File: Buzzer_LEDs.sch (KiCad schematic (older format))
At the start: 15 parts, among them Q1 2N7002BK, Q2 2N7002BK

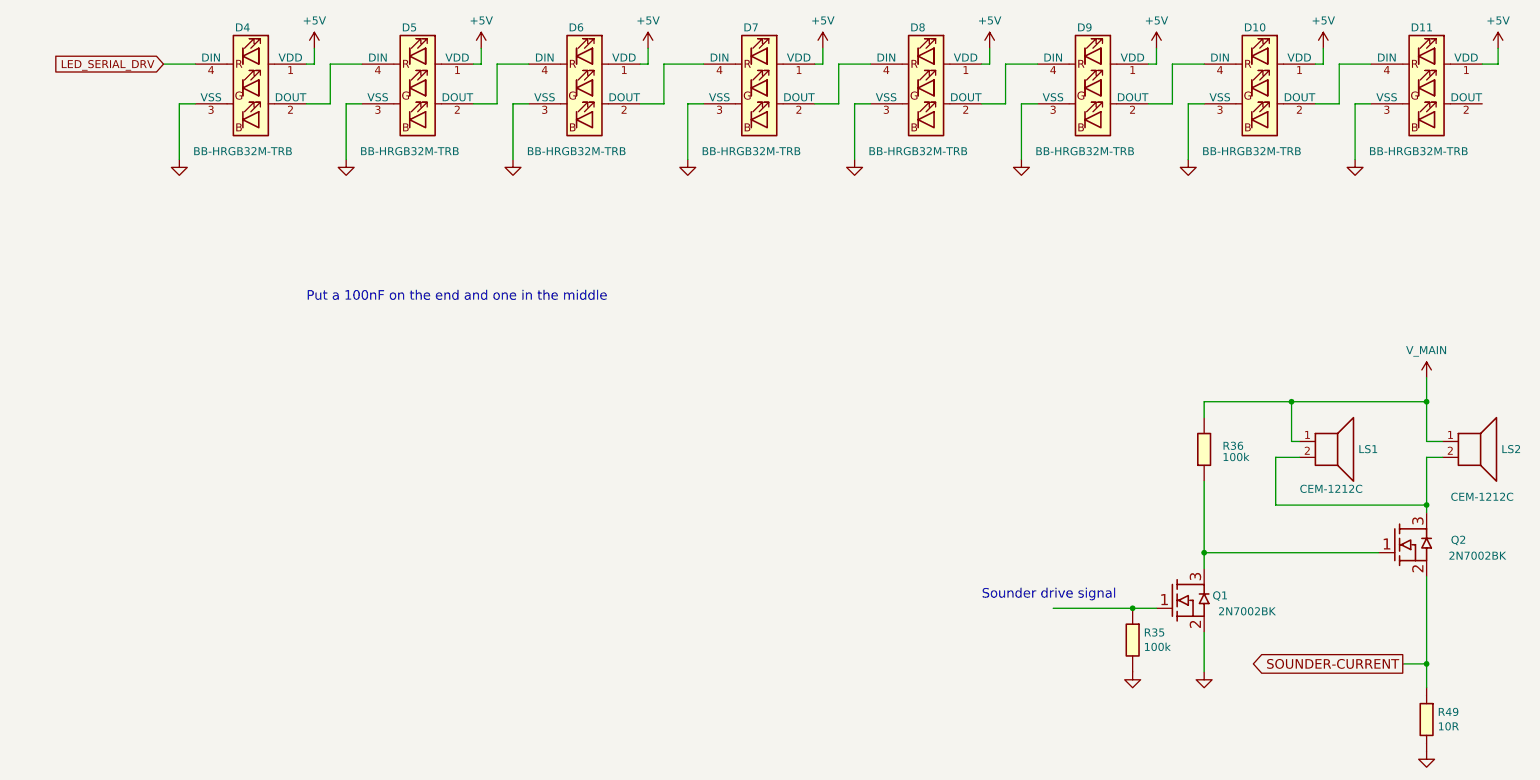
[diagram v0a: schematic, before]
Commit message: Went through the whole circuit and made a note of what needs changing
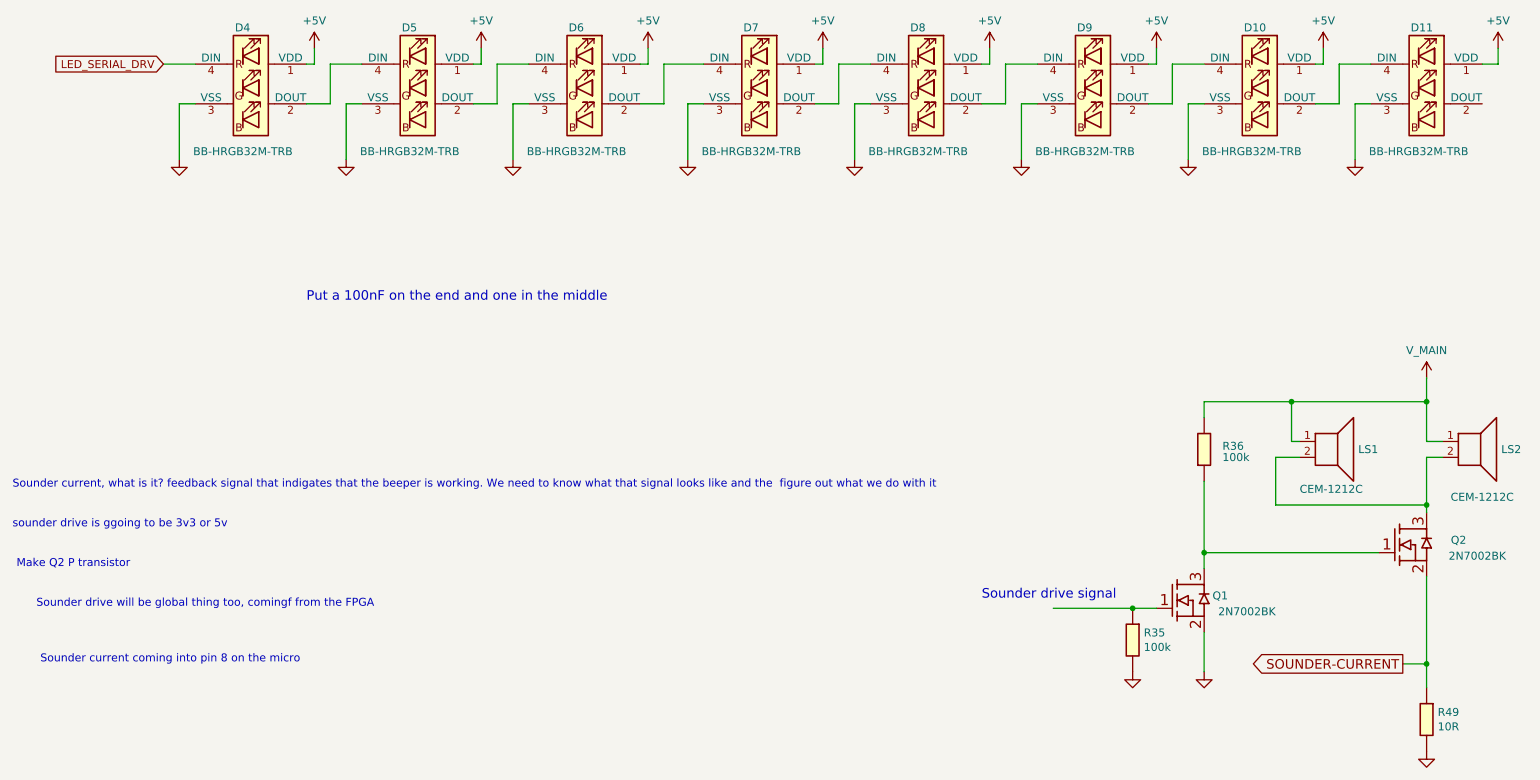
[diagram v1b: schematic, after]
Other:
- note added: "Make Q2 P transistor"
- note added: "Sounder current coming into pin 8 on the micro"
- note added: "Sounder current, what is it? feedback signal that indigates that the beeper is working. We need to know what that signal looks like and the figure out what we do with it"
- note added: "Sounder drive will be global thing too, comingf from the FPGA"
- note added: "sounder drive is ggoing to be 3v3 or 5v"
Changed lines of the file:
@@
 Text Notes 2750 3125 0    60   ~ 0
 Put a 100nF on the end and one in the middle\n
+Text Notes 900  4300 0    50   ~ 0
+Sounder current, what is it? feedback signal that indigates that the beeper is working. We need to know what that signal looks like and the  figure out what we do with it
+Text Notes 900  4550 0    50   ~ 0
+sounder drive is ggoing to be 3v3 or 5v
+Text Notes 925  4800 0    50   ~ 0
+Make Q2 P transistor
+Text Notes 1050 5050 0    50   ~ 0
+Sounder drive will be global thing too, comingf from the FPGA
+Text Notes 1075 5400 0    50   ~ 0
+Sounder current coming into pin 8 on the micro
 $EndSCHEMATC

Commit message: TLV75512 ON fpga jtag special PWR sheet 7 Changed Q2 on Buzzer LEDs sheet 8 from N type to P type
TLV75512 ON fpga jtag special PWR sheet 7
Changed Q2 on Buzzer LEDs sheet 8 from N type to P type
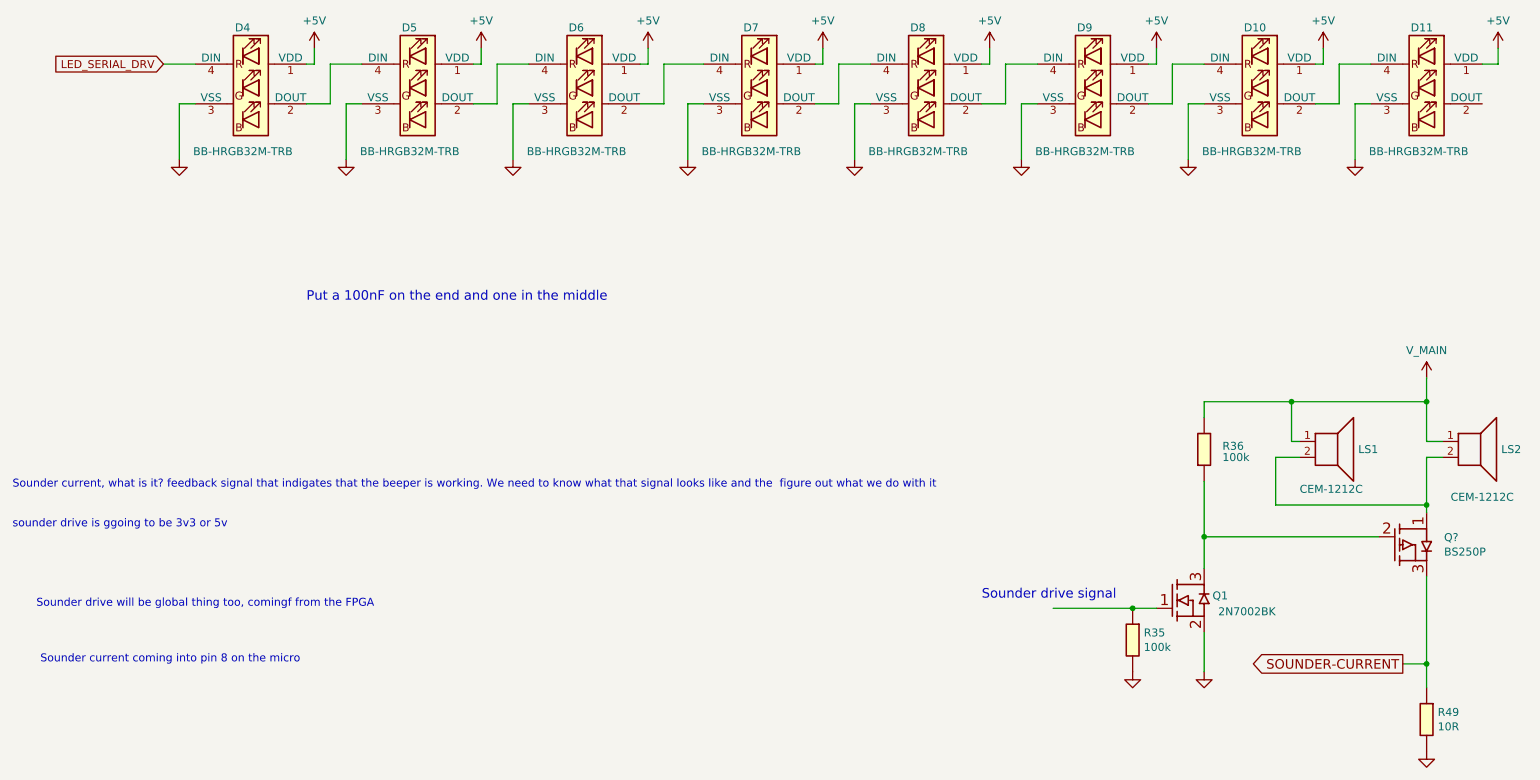
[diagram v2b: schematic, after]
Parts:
- removed Q2: 2N7002BK, Package_TO_SOT_SMD:SOT-23, symbol OpenVent:2N7002BK
- added Q?: BS250P, symbol OpenVent:BS250P
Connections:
- net SOUNDER-CURRENT: now also Q?.3 (D)
- net at Q1.3 (D), R36.1: now also Q?.2 (G1)
- net at LS1.2, LS2.2: now also Q?.1 (S)
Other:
- note removed: "Make Q2 P transistor"
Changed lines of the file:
@@
 	9800 4850 9800 5400
-Wire Wire Line
-	8400 4700 9500 4700
-Wire Wire Line
-	8400 4250 8400 4700
 Wire Wire Line
 	8400 3750 8400 3850
@@
 Wire Wire Line
 	8400 5450 8400 5200
-Wire Wire Line
-	8400 4800 8400 4700
 Text Notes 7000 5000 0    60   ~ 0
 Sounder drive signal
-Connection ~ 8400 4700
 Connection ~ 8950 3750
 Connection ~ 9800 5400
 Connection ~ 9800 3750
-$Comp
-L OpenVent:2N7002BK Q?
-U 1 1 5FCC52D3
-P 9800 4450
-AR Path="/5F8F894A/5FCC52D3" Ref="Q?"  Part="1"
-AR Path="/5FCA4074/5FCC52D3" Ref="Q2"  Part="1"
-F 0 "Q2" H 9550 4250 50  0000 L BNN
-F 1 "2N7002BK" H 9300 4150 50  0000 L BNN
-F 2 "Package_TO_SOT_SMD:SOT-23" H 9750 4100 50  0001 C CNN
-F 3 "https://assets.nexperia.com/documents/data-sheet/2N7002BK.pdf" H 9750 4100 50  0001 C CNN
-F 4 "350mA" H 9800 4450 50  0001 C CNN "Current"
-F 5 "MOSFET N-CH 60V 350MA SOT23" H 9800 4450 50  0001 C CNN "Desc"
-F 6 "N-Channel 350mA (Ta) 370mW (Ta) Surface Mount TO-236AB" H 9800 4450 50  0001 C CNN "Detailed"
-F 7 "DigiKey" H 9800 4450 50  0001 C CNN "DistName"
-F 8 "1727-4789-2-ND" H 9800 4450 50  0001 C CNN "Dist_PN"
-F 9 "Nexperia USA Inc." H 9800 4450 50  0001 C CNN "Mfr"
-F 10 "2N7002BK,215" H 9800 4450 50  0001 C CNN "Mfr_PN"
-F 11 "60V" H 9800 4450 50  0001 C CNN "Voltage"
-	1    9800 4450
-	-1   0    0    -1
-$EndComp
 $Comp
 L OpenVent:100K_0603_Chip_Resistor,_1%,_0.1W R?
@@
 Text Notes 900  4550 0    50   ~ 0
 sounder drive is ggoing to be 3v3 or 5v
-Text Notes 925  4800 0    50   ~ 0
-Make Q2 P transistor
 Text Notes 1050 5050 0    50   ~ 0
 Sounder drive will be global thing too, comingf from the FPGA
 Text Notes 1075 5400 0    50   ~ 0
 Sounder current coming into pin 8 on the micro
+$Comp
+L OpenVent:BS250P Q?
+U 1 1 5FF708AD
+P 9800 4850
+F 0 "Q?" H 9690 4604 50  0000 R CNN
+F 1 "BS250P" H 9690 4695 50  0000 R CNN
+F 2 "" H 9800 4850 50  0000 C CNN
+F 3 "" H 9800 4850 50  0000 C CNN
+	1    9800 4850
+	-1   0    0    1
+$EndComp
+Wire Wire Line
+	8400 4250 8400 4600
+Wire Wire Line
+	9500 4600 8400 4600
+Connection ~ 8400 4600
+Wire Wire Line
+	8400 4600 8400 4800
 $EndSCHEMATC
